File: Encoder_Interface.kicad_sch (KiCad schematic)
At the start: 0 parts

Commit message: Wired the AS5047P Encoder to the STM32 for reading the Stepper position
Signed-off-by: Vincent Cadicamo <vcadicamo@icloud.com>
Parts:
- added C25: 100n, Capacitor_SMD:C_0402_1005Metric, symbol Device:C
- added U5: AS5047P-ATSM, TSSOP14_OSM, symbol Stepper_ESC:AS5047P-ATSM
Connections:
- new net +3.3V: C25.2, U5.11 (VDD), U5.12 (VDD3V)
- new net GND: C25.1, U5.13 (GND), U5.5 (TEST)
- new net PC9: U5.1 (CSn)
- new net SPI3_MISO: U5.3 (MISO)
- new net SPI3_MOSI: U5.4 (MOSI)
- new net SPI3_SCK: U5.2 (CLK)
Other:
- company: (none) -> RCCF
- title: (none) -> AS5047P

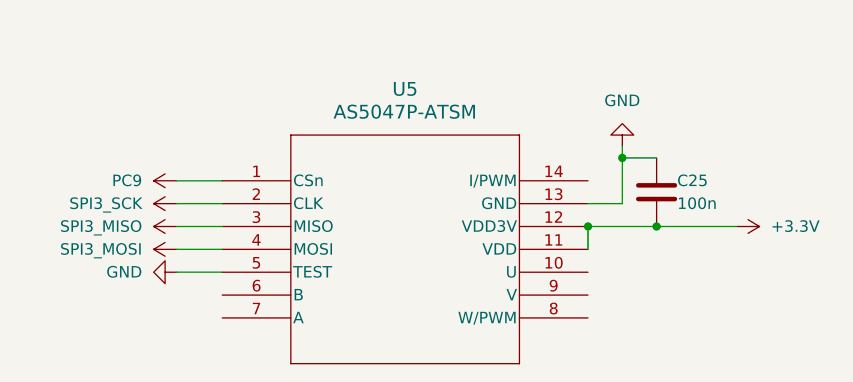
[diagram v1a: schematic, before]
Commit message: Added Hierarchical Labels connecting the SPI bus from the STM32 to the AS5047P
Signed-off-by: Vincent Cadicamo <vcadicamo@icloud.com>
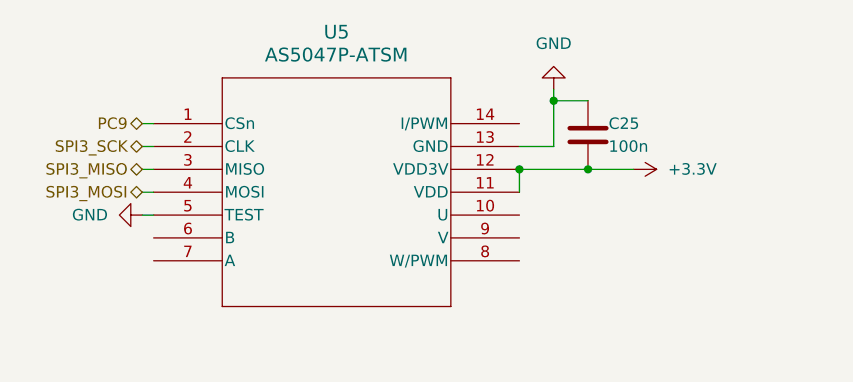
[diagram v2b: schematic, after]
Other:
- moved on the sheet: C25, U5
